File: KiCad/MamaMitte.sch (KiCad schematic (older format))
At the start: 5 parts, among them J1 WSCART

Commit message: Add footprints and assign nets
Assigned and placed footprints, and assigned nets to vias.
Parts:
- C1, C2, C3, C9: footprint (none) -> MamaMitte:C_0402_1005Metric
- J1: footprint (none) -> MamaMitte:WSCE-48_P1.25mm
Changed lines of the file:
@@
 F 0 "J1" H 9778 3653 60  0000 L CNN
 F 1 "WSCART" H 9778 3547 60  0000 L CNN
-F 2 "" H 7950 6450 60  0001 C CNN
+F 2 "MamaMitte:WSCE-48_P1.25mm" H 7950 6450 60  0001 C CNN
 F 3 "" H 7950 6450 60  0001 C CNN
 	1    9500 3600
@@
 	9250 3550 9250 3650
 $Comp
-L power:GND #PWR?
+L power:GND #PWR0101
 U 1 1 6085E72D
 P 8900 1250
-F 0 "#PWR?" H 8900 1000 50  0001 C CNN
+F 0 "#PWR0101" H 8900 1000 50  0001 C CNN
 F 1 "GND" H 8905 1077 50  0000 C CNN
 F 2 "" H 8900 1250 50  0001 C CNN
@@
 	9250 1250 8900 1250
 $Comp
-L power:GND #PWR?
+L power:GND #PWR0102
 U 1 1 6085F72B
 P 8900 5950
-F 0 "#PWR?" H 8900 5700 50  0001 C CNN
+F 0 "#PWR0102" H 8900 5700 50  0001 C CNN
 F 1 "GND" H 8905 5777 50  0000 C CNN
 F 2 "" H 8900 5950 50  0001 C CNN
@@
 	8900 3550 9250 3550
 $Comp
-L power:+3.3V #PWR?
+L power:+3.3V #PWR0103
 U 1 1 60857AB1
 P 8900 3550
-F 0 "#PWR?" H 8900 3400 50  0001 C CNN
+F 0 "#PWR0103" H 8900 3400 50  0001 C CNN
 F 1 "+3.3V" H 8915 3723 50  0000 C CNN
 F 2 "" H 8900 3550 50  0001 C CNN
@@
 	8625 5100 8625 6025
 $Comp
-L power:+3.3V #PWR?
+L power:+3.3V #PWR0104
 U 1 1 60A3D4C7
 P 7825 5400
-F 0 "#PWR?" H 7825 5250 50  0001 C CNN
+F 0 "#PWR0104" H 7825 5250 50  0001 C CNN
 F 1 "+3.3V" H 7840 5573 50  0000 C CNN
 F 2 "" H 7825 5400 50  0001 C CNN
@@
 $EndComp
 $Comp
-L power:+3.3V #PWR?
+L power:+3.3V #PWR0105
 U 1 1 60A3D1EE
 P 7350 5400
-F 0 "#PWR?" H 7350 5250 50  0001 C CNN
+F 0 "#PWR0105" H 7350 5250 50  0001 C CNN
 F 1 "+3.3V" H 7365 5573 50  0000 C CNN
 F 2 "" H 7350 5400 50  0001 C CNN
@@
 $EndComp
 $Comp
-L power:+3.3V #PWR?
+L power:+3.3V #PWR0106
 U 1 1 60A3CC70
 P 6875 5400
-F 0 "#PWR?" H 6875 5250 50  0001 C CNN
+F 0 "#PWR0106" H 6875 5250 50  0001 C CNN
 F 1 "+3.3V" H 6890 5573 50  0000 C CNN
 F 2 "" H 6875 5400 50  0001 C CNN
@@
 $EndComp
 $Comp
-L power:GND #PWR?
+L power:GND #PWR0107
 U 1 1 60A3C7A0
 P 7825 5700
-F 0 "#PWR?" H 7825 5450 50  0001 C CNN
+F 0 "#PWR0107" H 7825 5450 50  0001 C CNN
 F 1 "GND" H 7830 5527 50  0000 C CNN
 F 2 "" H 7825 5700 50  0001 C CNN
@@
 $EndComp
 $Comp
-L power:GND #PWR?
+L power:GND #PWR0108
 U 1 1 60A3C452
 P 7350 5700
-F 0 "#PWR?" H 7350 5450 50  0001 C CNN
+F 0 "#PWR0108" H 7350 5450 50  0001 C CNN
 F 1 "GND" H 7355 5527 50  0000 C CNN
 F 2 "" H 7350 5700 50  0001 C CNN
@@
 $EndComp
 $Comp
-L power:GND #PWR?
+L power:GND #PWR0109
 U 1 1 60A3BF31
 P 6875 5700
-F 0 "#PWR?" H 6875 5450 50  0001 C CNN
+F 0 "#PWR0109" H 6875 5450 50  0001 C CNN
 F 1 "GND" H 6880 5527 50  0000 C CNN
 F 2 "" H 6875 5700 50  0001 C CNN
@@
 F 0 "C3" H 7940 5596 50  0000 L CNN
 F 1 "C103" H 7940 5505 50  0000 L CNN
-F 2 "" H 7863 5400 50  0001 C CNN
+F 2 "MamaMitte:C_0402_1005Metric" H 7863 5400 50  0001 C CNN
 F 3 "~" H 7825 5550 50  0001 C CNN
 	1    7825 5550
@@
 F 0 "C2" H 7465 5596 50  0000 L CNN
 F 1 "C105" H 7465 5505 50  0000 L CNN
-F 2 "" H 7388 5400 50  0001 C CNN
+F 2 "MamaMitte:C_0402_1005Metric" H 7388 5400 50  0001 C CNN
 F 3 "~" H 7350 5550 50  0001 C CNN
 	1    7350 5550
@@
 F 0 "C1" H 6990 5596 50  0000 L CNN
 F 1 "C105" H 6990 5505 50  0000 L CNN
-F 2 "" H 6913 5400 50  0001 C CNN
+F 2 "MamaMitte:C_0402_1005Metric" H 6913 5400 50  0001 C CNN
 F 3 "~" H 6875 5550 50  0001 C CNN
 	1    6875 5550
@@
 $EndSheet
 $Comp
-L power:+3.3V #PWR?
+L power:+3.3V #PWR0110
 U 1 1 60BD0153
 P 8275 5425
-F 0 "#PWR?" H 8275 5275 50  0001 C CNN
+F 0 "#PWR0110" H 8275 5275 50  0001 C CNN
 F 1 "+3.3V" H 8290 5598 50  0000 C CNN
 F 2 "" H 8275 5425 50  0001 C CNN
@@
 $EndComp
 $Comp
-L power:GND #PWR?
+L power:GND #PWR0111
 U 1 1 60BD0289
 P 8275 5725
-F 0 "#PWR?" H 8275 5475 50  0001 C CNN
+F 0 "#PWR0111" H 8275 5475 50  0001 C CNN
 F 1 "GND" H 8280 5552 50  0000 C CNN
 F 2 "" H 8275 5725 50  0001 C CNN
@@
 F 0 "C9" H 8390 5621 50  0000 L CNN
 F 1 "C103" H 8390 5530 50  0000 L CNN
-F 2 "" H 8313 5425 50  0001 C CNN
+F 2 "MamaMitte:C_0402_1005Metric" H 8313 5425 50  0001 C CNN
 F 3 "~" H 8275 5575 50  0001 C CNN
 	1    8275 5575

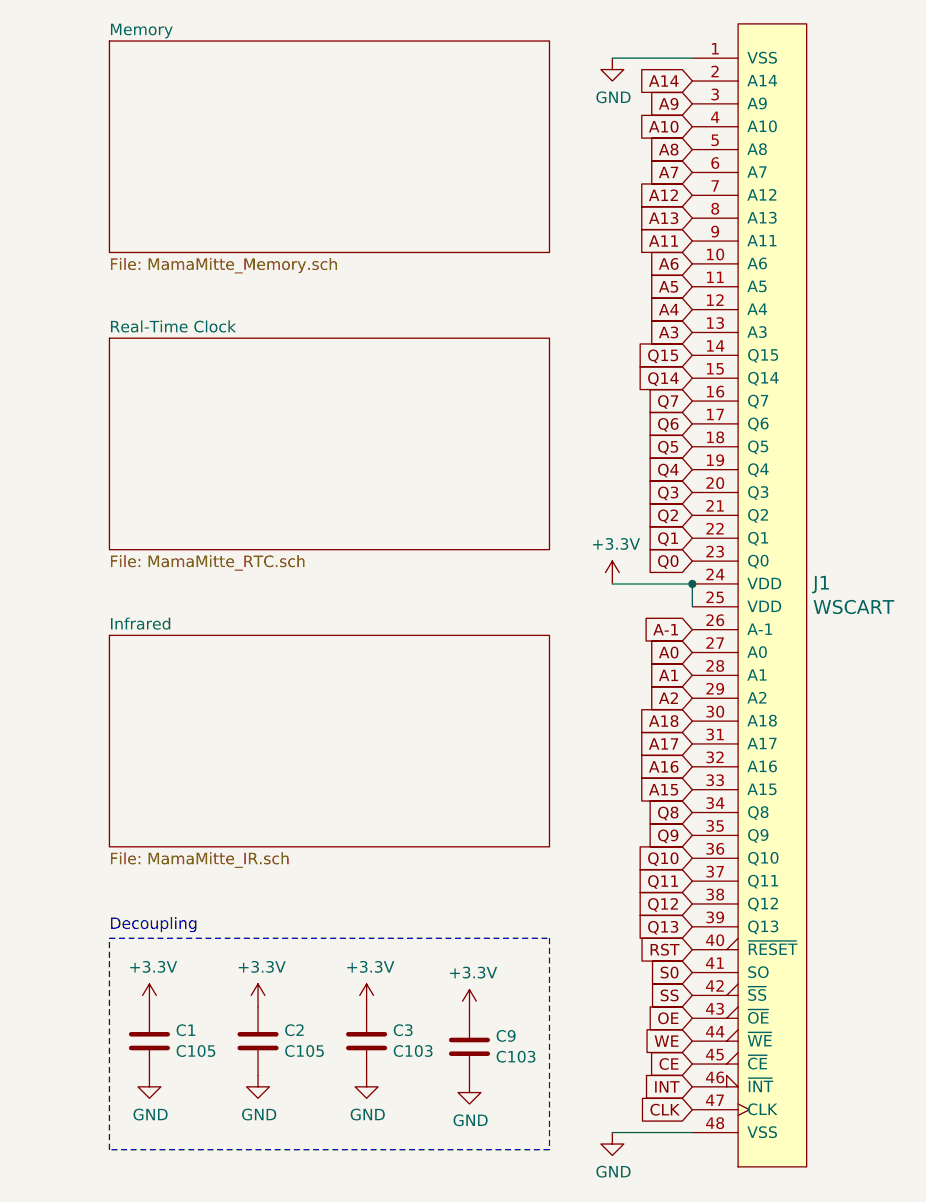
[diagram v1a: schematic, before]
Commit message: Update schematic
Change power source for RTC pull-ups, and restructure IR block.
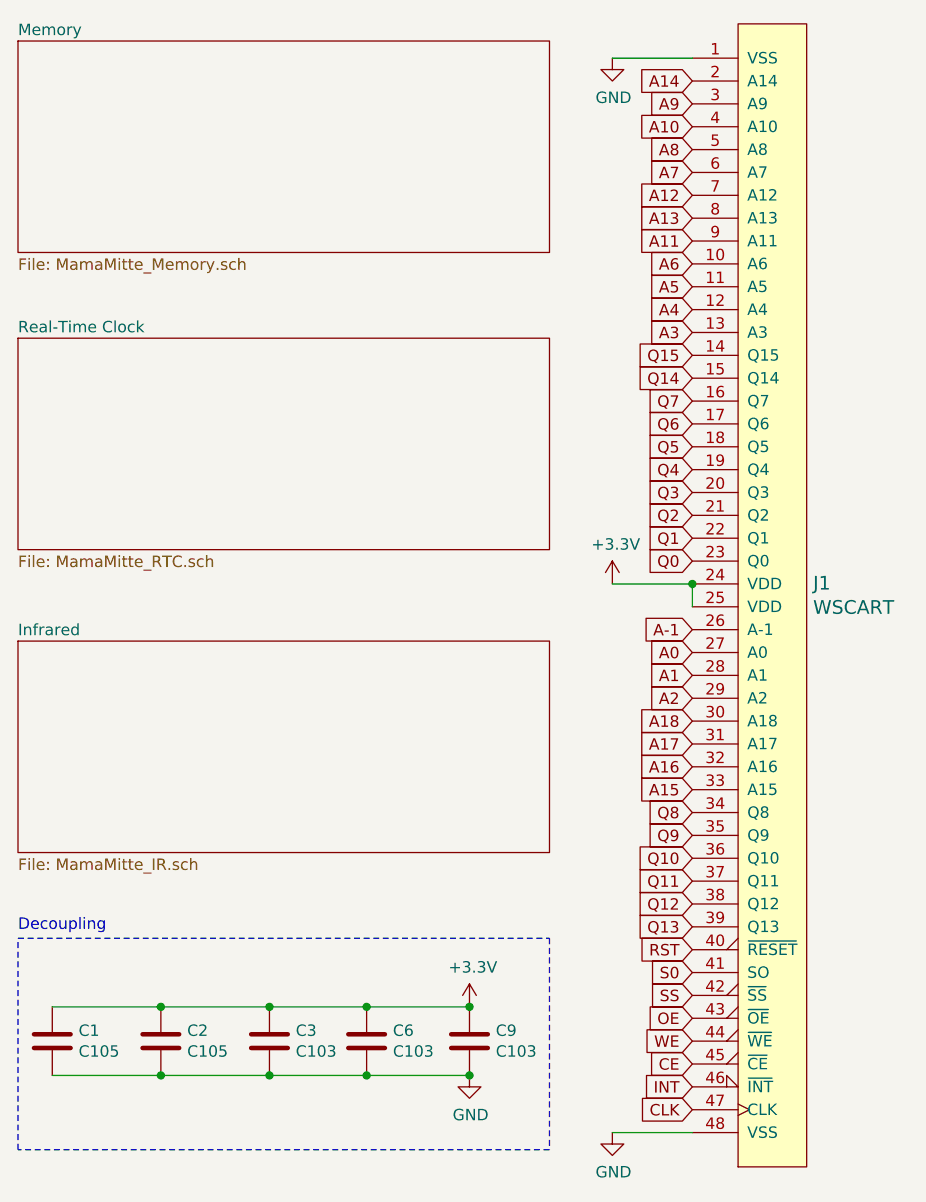
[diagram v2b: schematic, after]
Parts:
- added C6: C103, MamaMitte:C_0402_1005Metric, symbol Device:C
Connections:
- net +3V3: now also C6.1
- net GND: now also C6.2
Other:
- moved on the sheet: C1, C2, C3, C9
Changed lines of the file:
@@
 	1    0    0    -1
 $EndComp
-Text Notes 6700 5075 0    50   ~ 0
+Text Notes 6300 5075 0    50   ~ 0
 Decoupling
 Wire Notes Line
-	6700 5100 8625 5100
+	6300 5100 8625 5100
 Wire Notes Line
-	6700 6025 6700 5100
+	6300 6025 6300 5100
 Wire Notes Line
-	8625 6025 6700 6025
+	8625 6025 6300 6025
 Wire Notes Line
 	8625 5100 8625 6025
 $Comp
-L power:+3.3V #PWR0104
-U 1 1 60A3D4C7
-P 7825 5400
-F 0 "#PWR0104" H 7825 5250 50  0001 C CNN
-F 1 "+3.3V" H 7840 5573 50  0000 C CNN
-F 2 "" H 7825 5400 50  0001 C CNN
-F 3 "" H 7825 5400 50  0001 C CNN
-	1    7825 5400
+L Device:C C3
+U 1 1 60A3BA77
+P 7400 5550
+F 0 "C3" H 7515 5596 50  0000 L CNN
+F 1 "C103" H 7515 5505 50  0000 L CNN
+F 2 "MamaMitte:C_0402_1005Metric" H 7438 5400 50  0001 C CNN
+F 3 "~" H 7400 5550 50  0001 C CNN
+	1    7400 5550
 	1    0    0    -1
 $EndComp
 $Comp
-L power:+3.3V #PWR0105
-U 1 1 60A3D1EE
-P 7350 5400
-F 0 "#PWR0105" H 7350 5250 50  0001 C CNN
-F 1 "+3.3V" H 7365 5573 50  0000 C CNN
-F 2 "" H 7350 5400 50  0001 C CNN
-F 3 "" H 7350 5400 50  0001 C CNN
-	1    7350 5400
+L Device:C C2
+U 1 1 60A3B470
+P 6925 5550
+F 0 "C2" H 7040 5596 50  0000 L CNN
+F 1 "C105" H 7040 5505 50  0000 L CNN
+F 2 "MamaMitte:C_0402_1005Metric" H 6963 5400 50  0001 C CNN
+F 3 "~" H 6925 5550 50  0001 C CNN
+	1    6925 5550
 	1    0    0    -1
 $EndComp
 $Comp
-L power:+3.3V #PWR0106
-U 1 1 60A3CC70
-P 6875 5400
-F 0 "#PWR0106" H 6875 5250 50  0001 C CNN
-F 1 "+3.3V" H 6890 5573 50  0000 C CNN
-F 2 "" H 6875 5400 50  0001 C CNN
-F 3 "" H 6875 5400 50  0001 C CNN
-	1    6875 5400
+L Device:C C1
+U 1 1 60A3AFD5
+P 6450 5550
+F 0 "C1" H 6565 5596 50  0000 L CNN
+F 1 "C105" H 6565 5505 50  0000 L CNN
+F 2 "MamaMitte:C_0402_1005Metric" H 6488 5400 50  0001 C CNN
+F 3 "~" H 6450 5550 50  0001 C CNN
+	1    6450 5550
+	1    0    0    -1
+$EndComp
+$Sheet
+S 6300 2475 2325 925
+U 6088DF55
+F0 "Real-Time Clock" 50
+F1 "MamaMitte_RTC.sch" 50
+$EndSheet
+$Comp
+L Device:C C9
+U 1 1 60BD0293
+P 8275 5550
+F 0 "C9" H 8390 5596 50  0000 L CNN
+F 1 "C103" H 8390 5505 50  0000 L CNN
+F 2 "MamaMitte:C_0402_1005Metric" H 8313 5400 50  0001 C CNN
+F 3 "~" H 8275 5550 50  0001 C CNN
+	1    8275 5550
 	1    0    0    -1
 $EndComp
 $Comp
-L power:GND #PWR0107
-U 1 1 60A3C7A0
-P 7825 5700
-F 0 "#PWR0107" H 7825 5450 50  0001 C CNN
-F 1 "GND" H 7830 5527 50  0000 C CNN
-F 2 "" H 7825 5700 50  0001 C CNN
-F 3 "" H 7825 5700 50  0001 C CNN
-	1    7825 5700
-	1    0    0    -1
-$EndComp
-$Comp
-L power:GND #PWR0108
-U 1 1 60A3C452
-P 7350 5700
-F 0 "#PWR0108" H 7350 5450 50  0001 C CNN
-F 1 "GND" H 7355 5527 50  0000 C CNN
-F 2 "" H 7350 5700 50  0001 C CNN
-F 3 "" H 7350 5700 50  0001 C CNN
-	1    7350 5700
-	1    0    0    -1
-$EndComp
-$Comp
-L power:GND #PWR0109
-U 1 1 60A3BF31
-P 6875 5700
-F 0 "#PWR0109" H 6875 5450 50  0001 C CNN
-F 1 "GND" H 6880 5527 50  0000 C CNN
-F 2 "" H 6875 5700 50  0001 C CNN
-F 3 "" H 6875 5700 50  0001 C CNN
-	1    6875 5700
-	1    0    0    -1
-$EndComp
-$Comp
-L Device:C C3
-U 1 1 60A3BA77
+L Device:C C6
+U 1 1 60925867
 P 7825 5550
-F 0 "C3" H 7940 5596 50  0000 L CNN
+F 0 "C6" H 7940 5596 50  0000 L CNN
 F 1 "C103" H 7940 5505 50  0000 L CNN
 F 2 "MamaMitte:C_0402_1005Metric" H 7863 5400 50  0001 C CNN
@@
 	1    0    0    -1
 $EndComp
+Wire Wire Line
+	8275 5400 7825 5400
+Connection ~ 8275 5400
+Wire Wire Line
+	7825 5400 7400 5400
+Connection ~ 7825 5400
+Wire Wire Line
+	7400 5400 6925 5400
+Connection ~ 7400 5400
+Wire Wire Line
+	6925 5400 6450 5400
+Connection ~ 6925 5400
+Wire Wire Line
+	6450 5700 6925 5700
+Wire Wire Line
+	6925 5700 7400 5700
+Connection ~ 6925 5700
+Wire Wire Line
+	7400 5700 7825 5700
+Connection ~ 7400 5700
+Wire Wire Line
+	7825 5700 8275 5700
+Connection ~ 7825 5700
+Connection ~ 8275 5700
 $Comp
-L Device:C C2
-U 1 1 60A3B470
-P 7350 5550
-F 0 "C2" H 7465 5596 50  0000 L CNN
-F 1 "C105" H 7465 5505 50  0000 L CNN
-F 2 "MamaMitte:C_0402_1005Metric" H 7388 5400 50  0001 C CNN
-F 3 "~" H 7350 5550 50  0001 C CNN
-	1    7350 5550
-	1    0    0    -1
-$EndComp
-$Comp
-L Device:C C1
-U 1 1 60A3AFD5
-P 6875 5550
-F 0 "C1" H 6990 5596 50  0000 L CNN
-F 1 "C105" H 6990 5505 50  0000 L CNN
-F 2 "MamaMitte:C_0402_1005Metric" H 6913 5400 50  0001 C CNN
-F 3 "~" H 6875 5550 50  0001 C CNN
-	1    6875 5550
-	1    0    0    -1
-$EndComp
-$Sheet
-S 6700 2475 1925 925
-U 6088DF55
-F0 "Real-Time Clock" 50
-F1 "MamaMitte_RTC.sch" 50
-$EndSheet
-$Comp
-L power:+3.3V #PWR0110
-U 1 1 60BD0153
-P 8275 5425
-F 0 "#PWR0110" H 8275 5275 50  0001 C CNN
-F 1 "+3.3V" H 8290 5598 50  0000 C CNN
-F 2 "" H 8275 5425 50  0001 C CNN
-F 3 "" H 8275 5425 50  0001 C CNN
-	1    8275 5425
+L power:+3.3V #PWR?
+U 1 1 609288D6
+P 8275 5400
+F 0 "#PWR?" H 8275 5250 50  0001 C CNN
+F 1 "+3.3V" H 8290 5573 50  0000 C CNN
+F 2 "" H 8275 5400 50  0001 C CNN
+F 3 "" H 8275 5400 50  0001 C CNN
+	1    8275 5400
 	1    0    0    -1
 $EndComp
@@
 L power:GND #PWR0111
 U 1 1 60BD0289
-P 8275 5725
-F 0 "#PWR0111" H 8275 5475 50  0001 C CNN
-F 1 "GND" H 8280 5552 50  0000 C CNN
-F 2 "" H 8275 5725 50  0001 C CNN
-F 3 "" H 8275 5725 50  0001 C CNN
-	1    8275 5725
-	1    0    0    -1
-$EndComp
-$Comp
-L Device:C C9
-U 1 1 60BD0293
-P 8275 5575
-F 0 "C9" H 8390 5621 50  0000 L CNN
-F 1 "C103" H 8390 5530 50  0000 L CNN
-F 2 "MamaMitte:C_0402_1005Metric" H 8313 5425 50  0001 C CNN
-F 3 "~" H 8275 5575 50  0001 C CNN
-	1    8275 5575
+P 8275 5700
+F 0 "#PWR0111" H 8275 5450 50  0001 C CNN
+F 1 "GND" H 8280 5527 50  0000 C CNN
+F 2 "" H 8275 5700 50  0001 C CNN
+F 3 "" H 8275 5700 50  0001 C CNN
+	1    8275 5700
 	1    0    0    -1
 $EndComp
 $Sheet
-S 6700 3775 1925 925
+S 6300 3800 2325 925
 U 6088E26C
 F0 "Infrared" 50
@@
 $EndSheet
 $Sheet
-S 6700 1175 1925 925
+S 6300 1175 2325 925
 U 6086FA5B
 F0 "Memory" 50
